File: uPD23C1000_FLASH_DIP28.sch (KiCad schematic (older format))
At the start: 7 parts, among them J1 uPD23C1000, J2 Conn_1x2, J3 Conn_1x3, U1 GLS29EE010 (TSOP), U2 SST39SF010 (TSOP), U3 SST39SF010 / GLS29EE010 (PLCC)

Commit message: upD23C1000 add A17 & R2
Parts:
- added R2: 47k, 000_LOCAL:R_0805, symbol 000_LOCAL:R_US
- J2: footprint 000_LOCAL:Pin_Header_Angled_1x02_Pitch2.54mm -> 000_LOCAL:Pin_Header_Angled_1x02_Pitch2.54mm_shorted
- J3: footprint 000_LOCAL:Pin_Header_Angled_1x03_Pitch2.54mm -> 000_LOCAL:Pin_Header_Angled_1x03_Pitch2.54mm_12shorted; symbol Jumper:Jumper_3_Bridged12 -> 000_LOCAL:Jumper_3_Bridged12
- U1: value GLS29EE010 (TSOP) -> 29F0x0 (TSOP)
- U2: value SST39SF010 (TSOP) -> 29F0x0 (TSOP)
- U3: value SST39SF010 / GLS29EE010 (PLCC) -> 29F0x0 (PLCC)
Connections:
- net GND: now also R2.2
- net A17: now reaches U1.6 (NC)
- net A17: now also U2.6 (NC), U3.30 (NC), R2.1
- no-connect marks 0 -> 3
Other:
- note added: "DIP-28 legs"
- note added: "J2, J3: RUN vs PROGRAM configuration\n\nRUN configuration - for normal operation:\n* Install a jumper on J2\n* Install jumper on J3 in the A16 position\n\nPROGRAM configuration - for writing to the flash chip:\n* Remove the jumper from J2\n* Move the J3 jumper to the ~OE~ position\n* Insert the board into the programmer's ZIF socket, 2 rows away from the top.\nDon't close the ZIF clamping lever y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"
- note added: "OPTIONAL"
- note added: "PLCC-32 7x9"
- note added: "TSOP-32 20mm"
- note added: "U1 or U2 or U3: flash memory, 128K x 8, parallel, 5v\nExamples: SST39SF010, GLS29EE010, AM29F010\n\nOPTIONAL: If necessary, xxx020 part may be used in place of xxx010\nNormally: Install R1 and ex: SST39SF010\nAlternate: Install R1, R2, and ex: SST39SF020\n\nIn either case, only 128K of the chip is used.\nIn either case, configure the programmer for the xxx010 part, which may require overriding th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"
- note added: "sTSOP-32 14mm"
- note removed: "7x9pin PLCC32"
- note removed: "8x14mm TSOP32"
- note removed: "8x20mm TSOP32"
- note removed: "DIP28 legs"
- moved on the sheet: J1, J2, J3, R1, U1, U2, U3

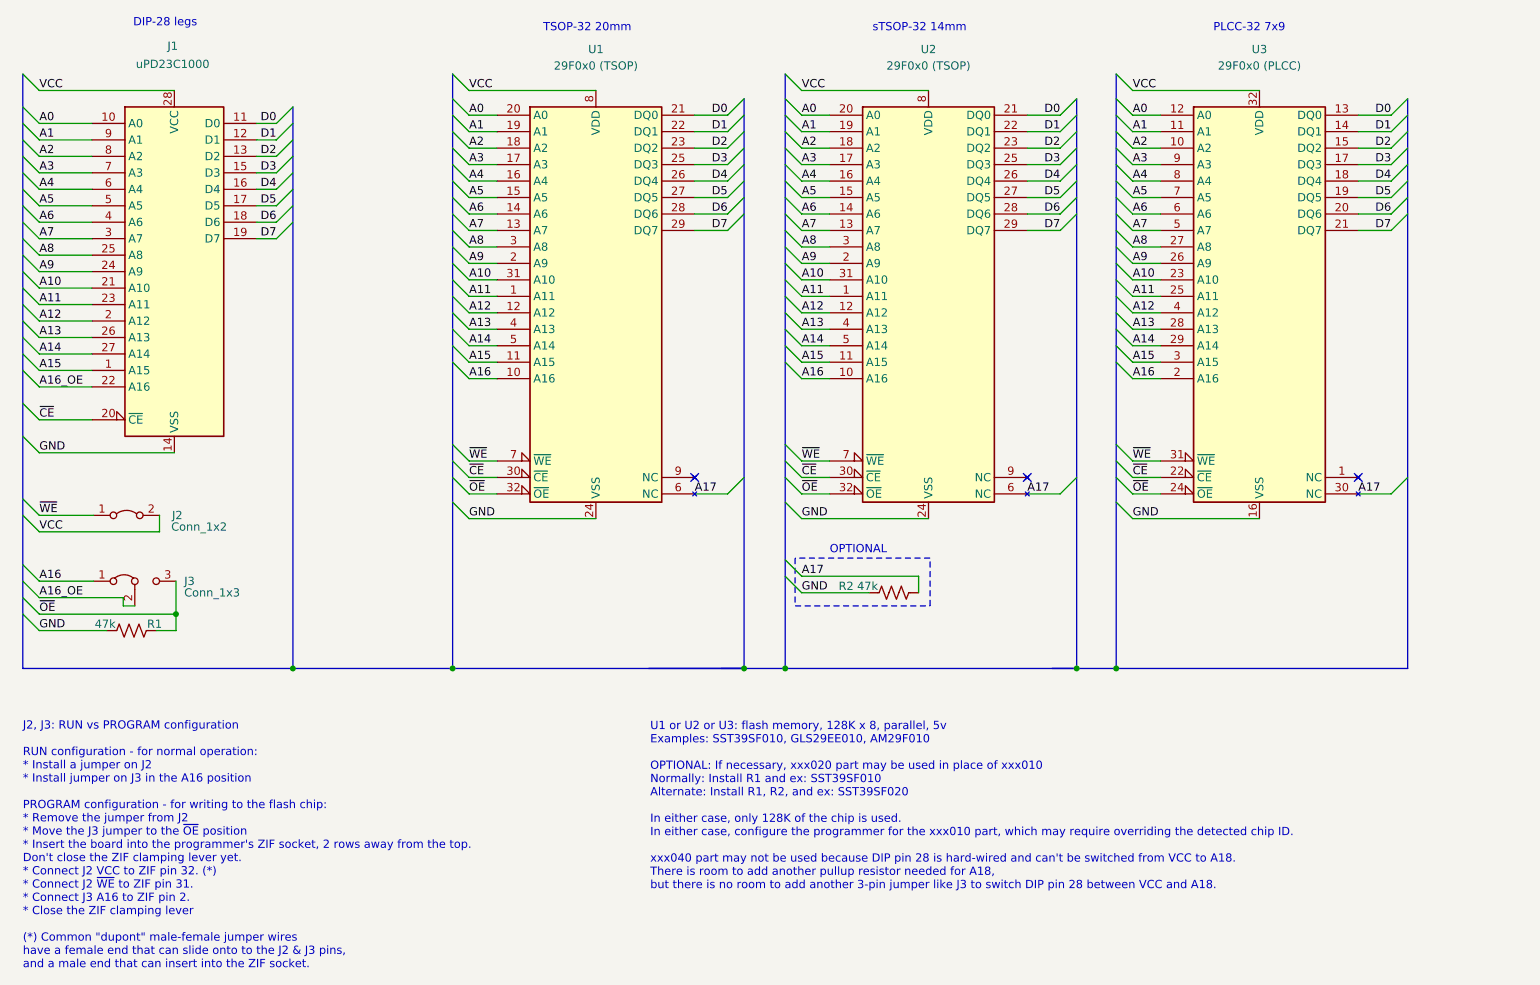
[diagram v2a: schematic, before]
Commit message: uPD23C1000 & FlashROM_8300 correct A17 & A18 handling
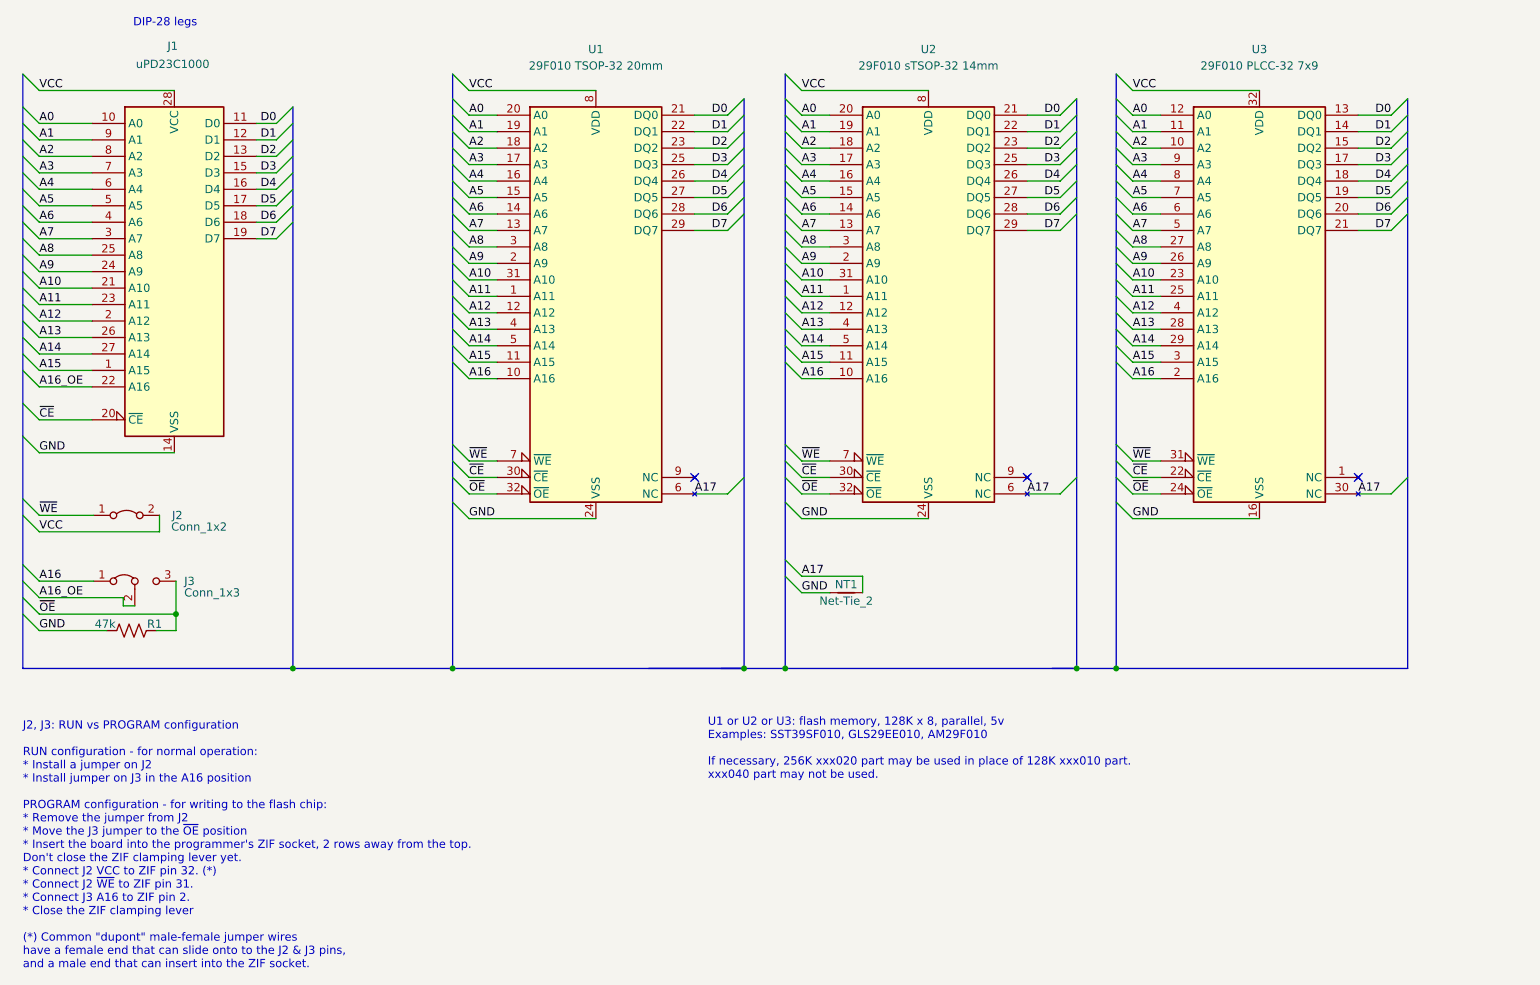
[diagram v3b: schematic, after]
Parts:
- removed R2: 47k, 000_LOCAL:R_0805, symbol 000_LOCAL:R_US
- added NT1: Net-Tie_2, 000_LOCAL:NetTie-2_SMD_0.18mm, symbol 000_LOCAL:Net-Tie_2
- U1: value 29F0x0 (TSOP) -> 29F010 TSOP-32 20mm
- U2: value 29F0x0 (TSOP) -> 29F010 sTSOP-32 14mm
- U3: value 29F0x0 (PLCC) -> 29F010 PLCC-32 7x9
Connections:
- net A17: now also NT1.2
- net GND: now also NT1.1
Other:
- note added: "U1 or U2 or U3: flash memory, 128K x 8, parallel, 5v\nExamples: SST39SF010, GLS29EE010, AM29F010\n\nIf necessary, 256K xxx020 part may be used in place of 128K xxx010 part.\nxxx040 part may not be used.\n"
- note removed: "OPTIONAL"
- note removed: "PLCC-32 7x9"
- note removed: "TSOP-32 20mm"
- note removed: "U1 or U2 or U3: flash memory, 128K x 8, parallel, 5v\nExamples: SST39SF010, GLS29EE010, AM29F010\n\nOPTIONAL: If necessary, xxx020 part may be used in place of xxx010\nNormally: Install R1 and ex: SST39SF010\nAlternate: Install R1, R2, and ex: SST39SF020\n\nIn either case, only 128K of the chip is used.\nIn either case, configure the programmer for the xxx010 part, which may require overriding th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"
- note removed: "sTSOP-32 14mm"
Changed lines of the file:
@@
 P 4680 2850
 F 0 "U1" H 4680 4450 50  0000 C CNN
-F 1 "29F0x0 (TSOP)" H 4680 4350 50  0000 C CNN
+F 1 "29F010 TSOP-32 20mm" H 4680 4350 50  0000 C CNN
 F 2 "000_LOCAL:TSOP32-20mm" H 4680 3150 50  0001 C CNN
 F 3 "http://ww1.microchip.com/downloads/en/DeviceDoc/25022B.pdf" H 4680 3150 50  0001 C CNN
@@
 P 6700 2850
 F 0 "U2" H 6700 4450 50  0000 C CNN
-F 1 "29F0x0 (TSOP)" H 6700 4350 50  0000 C CNN
+F 1 "29F010 sTSOP-32 14mm" H 6700 4350 50  0000 C CNN
 F 2 "000_LOCAL:TSOP32-14mm" H 6700 3150 50  0001 C CNN
 F 3 "http://ww1.microchip.com/downloads/en/DeviceDoc/25022B.pdf" H 6700 3150 50  0001 C CNN
@@
 P 8710 2850
 F 0 "U3" H 8710 4450 50  0000 C CNN
-F 1 "29F0x0 (PLCC)" H 8710 4350 50  0000 C CNN
+F 1 "29F010 PLCC-32 7x9" H 8710 4350 50  0000 C CNN
 F 2 "000_LOCAL:PLCC32_7x9" H 8710 3150 50  0001 C CNN
 F 3 "http://ww1.microchip.com/downloads/en/DeviceDoc/25022B.pdf" H 8710 3150 50  0001 C CNN
@@
 Text Notes 1870 1120 0    50   ~ 0
 DIP-28 legs
-Text Notes 4360 1150 0    50   ~ 0
-TSOP-32 20mm
-Text Notes 6360 1150 0    50   ~ 0
-sTSOP-32 14mm
-Text Notes 8430 1150 0    50   ~ 0
-PLCC-32 7x9
-Text Notes 5010 6360 0    50   ~ 0
-U1 or U2 or U3: flash memory, 128K x 8, parallel, 5v\nExamples: SST39SF010, GLS29EE010, AM29F010\n\nOPTIONAL: If necessary, xxx020 part may be used in place of xxx010\nNormally: Install R1 and ex: SST39SF010\nAlternate: Install R1, R2, and ex: SST39SF020\n\nIn either case, only 128K of the chip is used.\nIn either case, configure the programmer for the xxx010 part, which may require overriding the detected chip ID.\n\nxxx040 part may not be used because DIP pin 28 is hard-wired and can't be switched from VCC to A18.\nThere is room to add another pullup resistor needed for A18,\nbut there is no room to add another 3-pin jumper like J3 to switch DIP pin 28 between VCC and A18.\n
 Text Notes 1200 6840 0    50   ~ 0
 J2, J3: RUN vs PROGRAM configuration\n\nRUN configuration - for normal operation:\n* Install a jumper on J2\n* Install jumper on J3 in the A16 position\n\nPROGRAM configuration - for writing to the flash chip:\n* Remove the jumper from J2\n* Move the J3 jumper to the ~OE~ position\n* Insert the board into the programmer's ZIF socket, 2 rows away from the top.\nDon't close the ZIF clamping lever yet.\n* Connect J2 VCC to ZIF pin 32. (*)\n* Connect J2 ~WE~ to ZIF pin 31.\n* Connect J3 A16 to ZIF pin 2.\n* Close the ZIF clamping lever\n\n(*) Common "dupont" male-female jumper wires\nhave a female end that can slide onto to the J2 & J3 pins,\nand a male end that can insert into the ZIF socket.\n
@@
 Entry Wire Line
 	5830 4450 5930 4550
-$Comp
-L 000_LOCAL:R_US R2
-U 1 1 5FB60C5B
-P 6490 4550
-F 0 "R2" V 6450 4260 50  0000 C CNN
-F 1 "47k" V 6450 4390 50  0000 C CNN
-F 2 "000_LOCAL:R_0805" V 6530 4540 50  0001 C CNN
-F 3 "~" H 6490 4550 50  0001 C CNN
-	1    6490 4550
-	0    1    1    0
-$EndComp
 Entry Wire Line
 	5830 4350 5930 4450
 Wire Wire Line
-	5930 4450 6640 4450
+	5930 4450 6300 4450
 Text Label 5930 4450 0    50   ~ 0
 A17
 Wire Wire Line
-	5930 4550 6340 4550
-Wire Wire Line
-	6640 4550 6640 4450
-Wire Notes Line
-	6710 4340 5890 4340
-Text Notes 6100 4320 0    50   ~ 0
-OPTIONAL
+	5930 4550 6100 4550
+Wire Wire Line
+	6300 4550 6300 4450
 NoConn ~ 7300 3850
 NoConn ~ 9310 3850
 NoConn ~ 5280 3850
-Wire Notes Line
-	5890 4340 5890 4630
-Wire Notes Line
-	5890 4630 6710 4630
-Wire Notes Line
-	6710 4630 6710 4340
+Text Notes 5360 5690 0    50   ~ 0
+U1 or U2 or U3: flash memory, 128K x 8, parallel, 5v\nExamples: SST39SF010, GLS29EE010, AM29F010\n\nIf necessary, 256K xxx020 part may be used in place of 128K xxx010 part.\nxxx040 part may not be used.\n
+$Comp
+L 000_LOCAL:Net-Tie_2 NT1
+U 1 1 5FA78AD5
+P 6200 4550
+F 0 "NT1" H 6200 4600 50  0000 C CNN
+F 1 "Net-Tie_2" H 6200 4500 50  0000 C CNN
+F 2 "000_LOCAL:NetTie-2_SMD_0.18mm" H 6200 4550 50  0001 C CNN
+F 3 "~" H 6200 4550 50  0001 C CNN
+	1    6200 4550
+	1    0    0    -1
+$EndComp
 Wire Bus Line
 	5580 1550 5580 5010
